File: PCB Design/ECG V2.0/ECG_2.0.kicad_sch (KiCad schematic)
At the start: 54 parts, among them J1 01x05_Female, J2 JST_01x04_Male, U1 Li-Po, U10 ESP32-C3-MINI-1-N4, U11 FS8205A, U12 DW01, U2 TP4056-C21417, U3 USBLC6-2SC6, U4 Battery_Switch, U5 5V_switch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

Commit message: Gerber files and Larger pcb due to manufacturing limits
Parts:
- C1, C10: Note (none) -> https://jlcpcb.com/parts/componentSearch?searchTxt=0805B104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; Vendor (none) -> C38141
- C11, C2, C3, C8, C9: Note (none) -> https://jlcpcb.com/partdetail/2065-CL21A106KOQNNNE/C1713; Vendor (none) -> C1713
- C12, C13, C5: Note (none) -> https://jlcpcb.com/partdetail/39123-0805B104K500NT/C38141; Vendor (none) -> C38141
- C4: value 0.1uF -> 100nF; Note (none) -> https://jlcpcb.com/parts/componentSearch?searchTxt=0805B104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; Vendor (none) -> C38141
- C6: Note (none) -> https://jlcpcb.com/partdetail/TaiyoYuden-UMK212BBJ475KGT/C4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; Vendor (none) -> C412634
- C7: Note (none) -> https://jlcpcb.com/partdetail/168956-0805CG100J500NT/C157608; Vendor (none) -> C157608
- D1: Note (none) -> https://jlcpcb.com/partdetail/85432-NCD0603R1/C84263; Vendor (none) -> C84263
- D2: Note (none) -> https://jlcpcb.com/partdetail/YongyuPhotoelectric-SZYY0603G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; Vendor (none) -> C434420
- D3: Note (none) -> https://jlcpcb.com/partdetail/EverlightElec-19_117_BHC_ZL1M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; Vendor (none) -> C264469
- D4: Note (none) -> https://jlcpcb.com/partdetail/85434-NCD0603W1/C84265; Vendor (none) -> C84265
- J1: now left out of the parts list
- J2: footprint Connector_PinHeader_2.54mm:PinHeader_1x05_P2.54mm_Vertical -> Connector_PinHeader_2.54mm:PinHeader_1x04_P2.54mm_Vertical; Note (none) -> https://jlcpcb.com/partdetail/Zhouri-2_54_14/C5116483; Vendor (none) -> C5116483
- L1: Note (none) -> https://jlcpcb.com/partdetail/ShouHan-CY43_22UH/C2929416; Vendor (none) -> C2929416
- R1, R12, R2, R3, R6, R8: Note (none) -> https://jlcpcb.com/partdetail/18102-0805W8F1002T5E/C17414; Vendor (none) -> C17414
- R10, R9: Note (none) -> https://jlcpcb.com/partdetail/116585-RS05K512JT/C115337; Vendor (none) -> C115337
- R11: Note (none) -> https://jlcpcb.com/partdetail/116671-RS05K101JT/C115423; Vendor (none) -> C115423
- R4, R7: Note (none) -> https://jlcpcb.com/partdetail/Yageo-RC0805JR07220RL/C114742; Vendor (none) -> C114742
- R5: Note (none) -> https://jlcpcb.com/partdetail/4717-0805W8F1501T5E/C4310; Vendor (none) -> C4310
- Rprog1: Note (none) -> https://jlcpcb.com/partdetail/18076-0805W8F1401T5E/C17388; Vendor (none) -> C17388
- U10: MAXIMUM_PACKAGE_HEIGHT 2.55mm -> (none); Note (none) -> https://jlcpcb.com/partdetail/EspressifSystems-ESP32_C3_MIN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; Vendor (none) -> C2838502
- U11: Note (none) -> https://jlcpcb.com/partdetail/Fuxinsemi-FS8205A/C908265; Vendor (none) -> C908265
- U12: Note (none) -> https://jlcpcb.com/partdetail/GuangdongHottech-DW01/C181096; Vendor (none) -> C181096
- U2: Note (none) -> https://jlcpcb.com/partdetail/22134-TP4056M/C21417; Vendor (none) -> C21417
- U3: Note (none) -> https://jlcpcb.com/partdetail/TechPublic-USBLC62SC6/C2827654; Vendor (none) -> C2827654
- U4, U5, U7: Note (none) -> https://jlcpcb.com/partdetail/Korean_HropartsElec-SS_12D02V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; Vendor (none) -> C136719
- U6: Note (none) -> https://jlcpcb.com/partdetail/TexasInstruments-TLV62568DBVR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; Vendor (none) -> C163219
- U8: Note (none) -> https://jlcpcb.com/partdetail/eswitch-TL3301AF160QG/C273519; Vendor (none) -> C273519
- U9: Note (none) -> https://jlcpcb.com/partdetail/Shenzhen_KinghelmElec-KH_TYPE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; Vendor (none) -> C709357

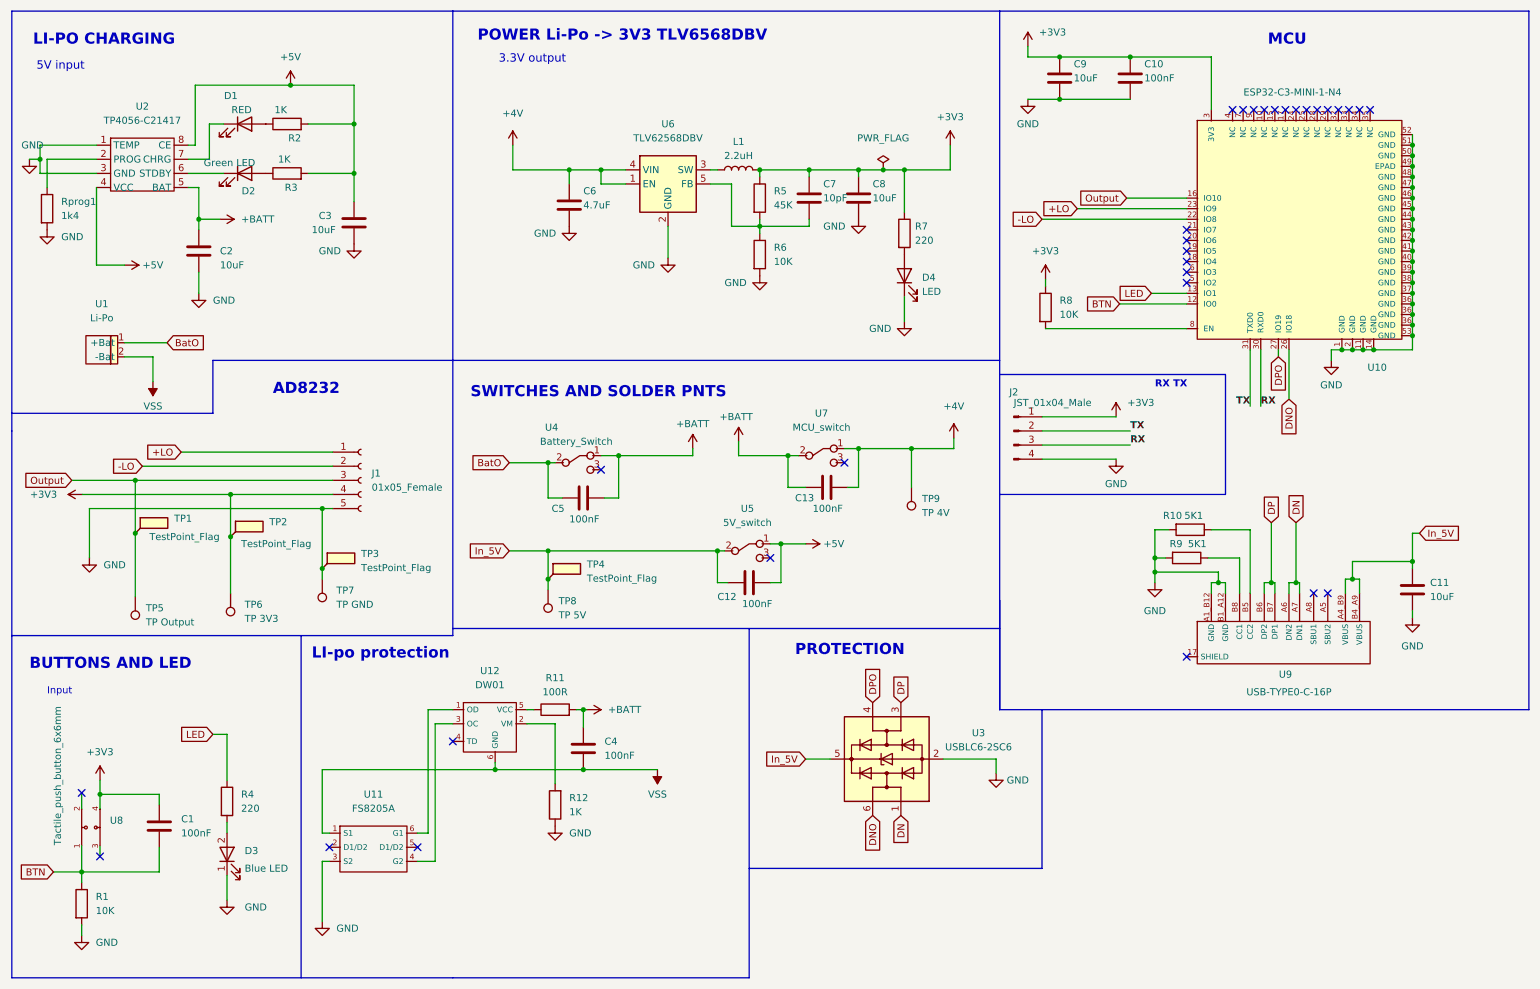
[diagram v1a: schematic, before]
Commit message: updated Schematic to reflect hardware testing issues
Changed schematic for USB-C, had the pin our wrong.

Changed through hole switch components and USB-C through hole for better fit.
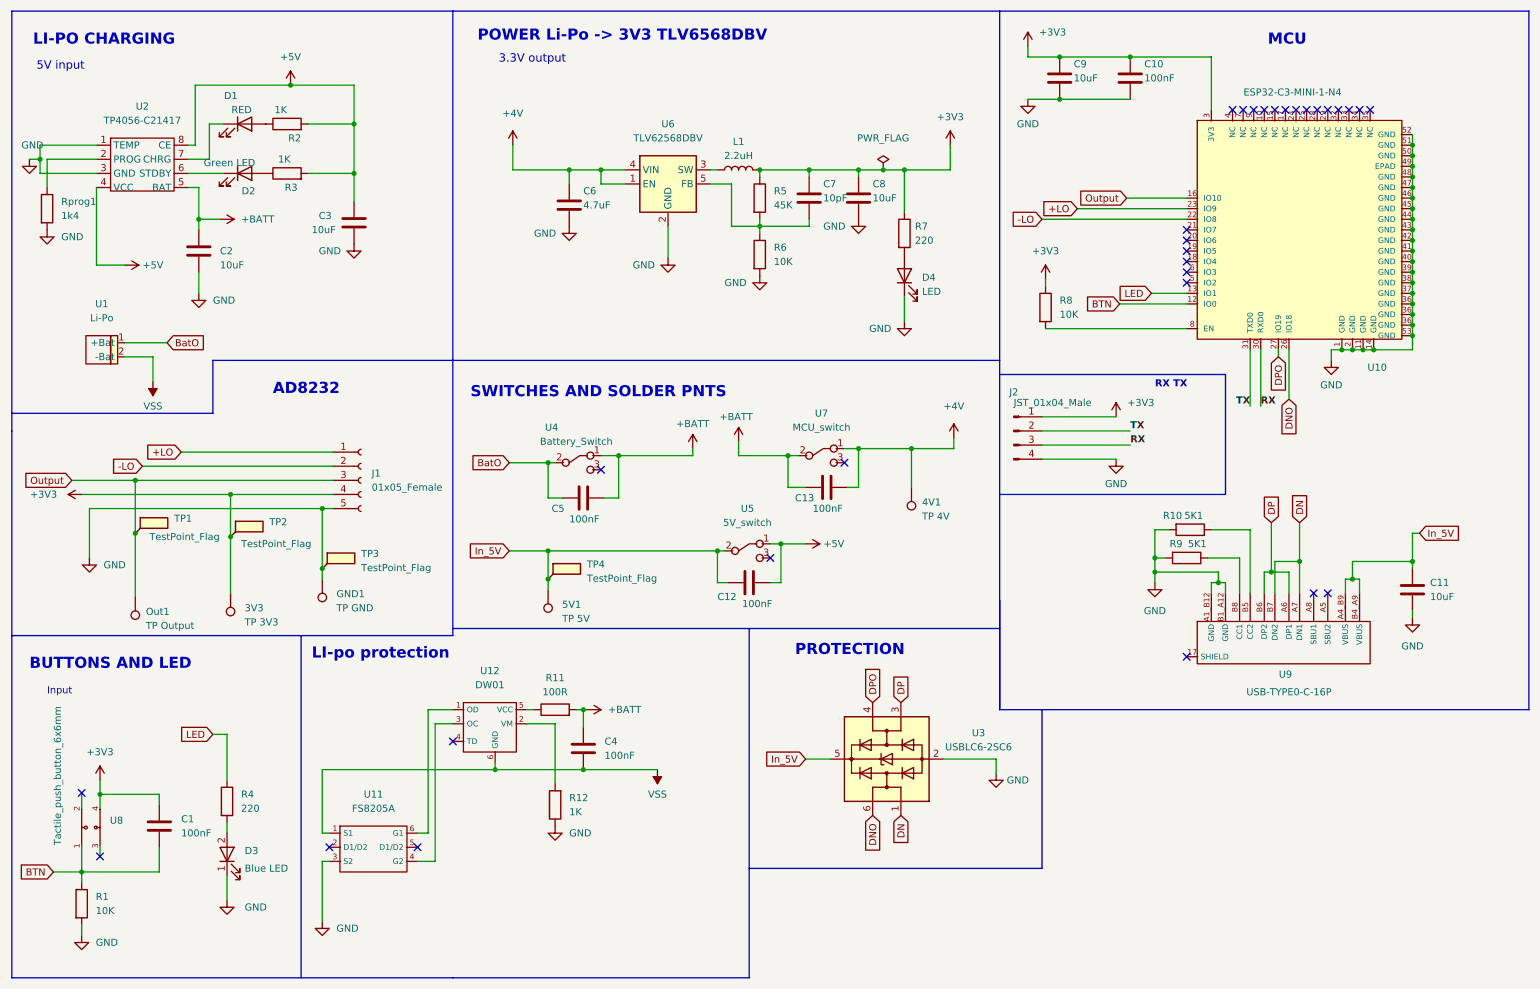
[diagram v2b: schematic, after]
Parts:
- renumbered TP6 to 3V3, TP9 to 4V1, TP8 to 5V1, TP7 to GND1, TP5 to Out1
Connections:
- net DN: now also U9.B7 (DN2); no longer U9.A6 (DN2)
- net DP: now also U9.A6 (DP1); no longer U9.B7 (DP1)
